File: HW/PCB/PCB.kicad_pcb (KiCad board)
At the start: 2 copper layers, 48 parts, among them J1 USB4105-GF-A, J2 DC_Jack, J4 Micro_SD_Card_Det_Hirose_DM3AT, Q1 2PC4081R, Q2 2PC4081R, SW1 ssss213202, SW2 SKRPACE010, SW3 SKRPACE010, U1 SCD40-D-R2, U2 FT231XS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

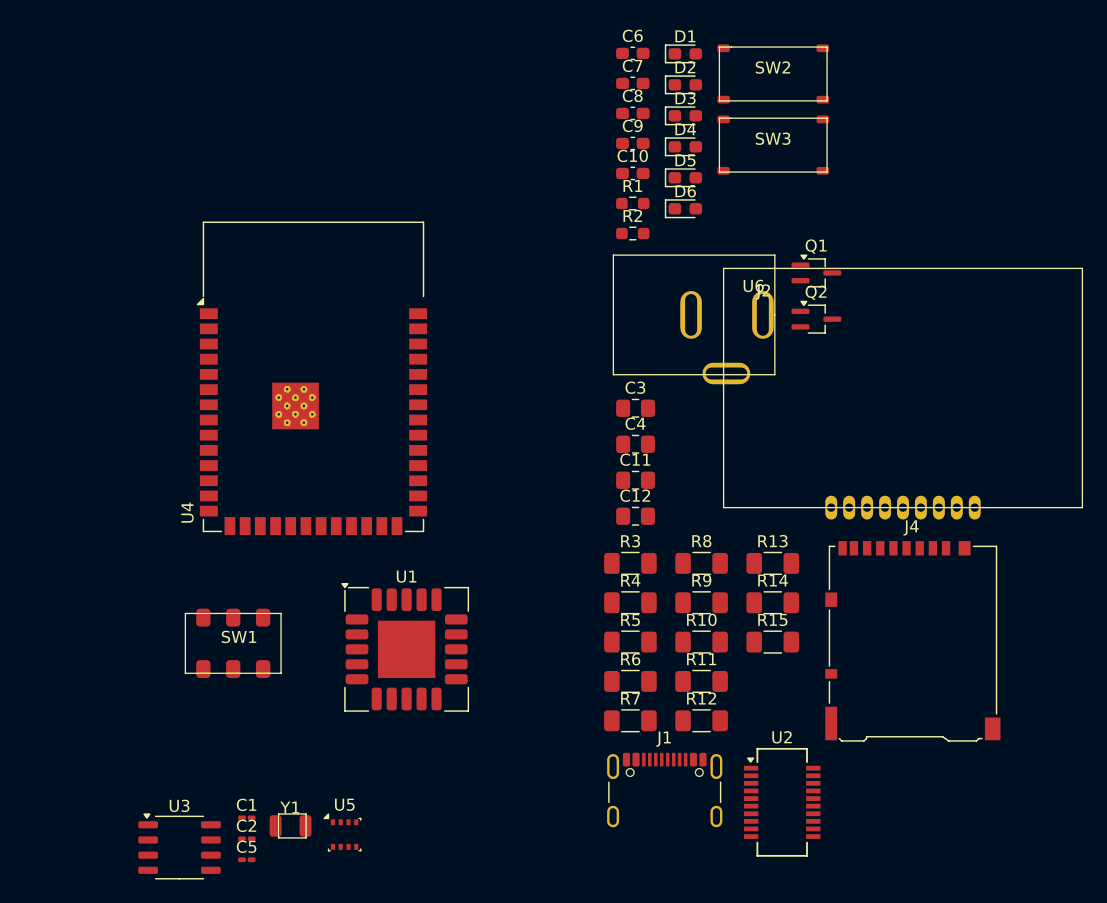
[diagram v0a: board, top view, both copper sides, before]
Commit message: Add PCB layout
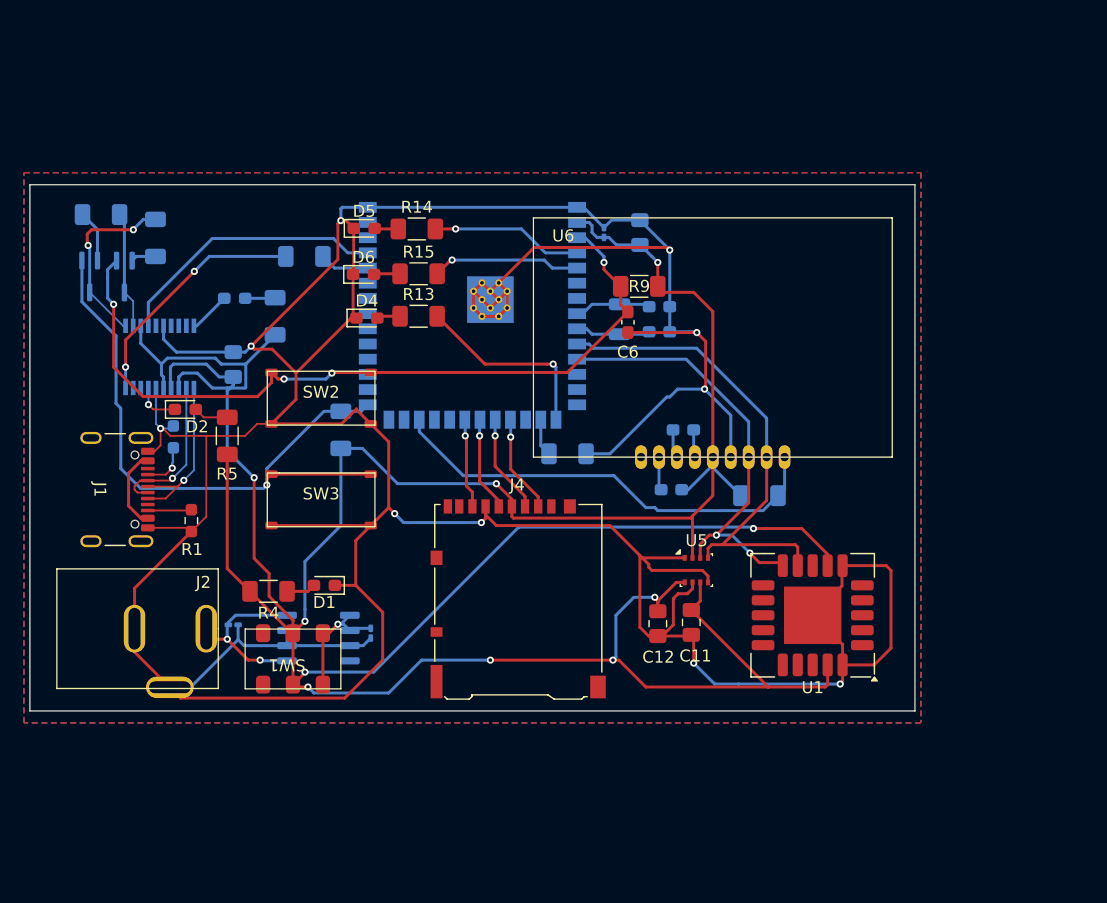
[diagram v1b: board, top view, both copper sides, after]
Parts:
- C1, C10, C2, C3, C4, C5, C7, C8, C9, D3, Q1, Q2, R10, R11, R12, R2, R3, R6, R7, R8, U2, U3, U4, Y1: moved to B.Cu
- moved U2 64.0 mm to (99.4, 84.4), turned to -90 degrees
- moved Q2 60.9 mm to (93.5, 77.7), turned to -90 degrees
- moved C5 60.3 mm to (136.5, 74.0), turned to 90 degrees
- moved R8 58.1 mm to (94.5, 72.5)
- moved Q1 57.9 mm to (96.4, 77.7), turned to -90 degrees
- moved R7 56.6 mm to (99.0, 74.5), turned to 90 degrees
- moved J1 53.8 mm to (94.7, 95.5), turned to -90 degrees
- moved D1 53.7 mm to (113.1, 103.5), turned to 180 degrees
- moved J2 53.4 mm to (103.2, 107.1)
- moved Y1 50.5 mm to (137.8, 81.2), turned to 90 degrees
- moved D2 49.8 mm to (101.5, 88.8)
- moved SW3 48.0 mm to (112.8, 96.3)
- moved SW2 46.5 mm to (112.8, 87.8)
- moved R1 45.4 mm to (102.0, 98.1), turned to -90 degrees
- moved R14 43.2 mm to (120.8, 73.7)
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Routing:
- net GND: track 0.00 -> 372.9 mm, vias 0 -> 10
- net +3V3: track 0.00 -> 300.2 mm, vias 0 -> 10
- net ESP32_EN: track 0.00 -> 65.7 mm, vias 0 -> 4
- net ESP32_IO0: track 0.00 -> 53.2 mm, vias 0 -> 1
- net ESP32_IO17_SCL: track 0.00 -> 40.6 mm
- net ESP32_IO47: track 0.00 -> 37.7 mm
- net ESP32_IO18_SDA: track 0.00 -> 36.5 mm, vias 0 -> 2
- net ESP32_TXD: track 0.00 -> 23.0 mm
- net Net-(U2-TXD): track 0.00 -> 20.3 mm, vias 0 -> 2
- net ESP32_IO3: track 0.00 -> 16.1 mm, vias 0 -> 1
- net DTR: track 0.00 -> 15.5 mm, vias 0 -> 2
- net VDD: track 0.00 -> 14.5 mm, vias 0 -> 2
- net USB_DP: track 0.00 -> 14.2 mm, vias 0 -> 1
- net USB_DM: track 0.00 -> 13.0 mm, vias 0 -> 1
- net ESP32_IO4: track 0.00 -> 12.7 mm, vias 0 -> 1
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- added copper zone on B.Cu, net GND
- added copper zone on F.Cu, net GND
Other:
- board outline added: 74 x 44 mm
